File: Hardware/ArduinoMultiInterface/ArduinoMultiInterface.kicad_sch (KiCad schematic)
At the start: 27 parts, among them J1 PORT1, J2 I2C, J3 SPI, J4 SER, SW1 SW_RESET, U1 ATmega328-P, U2 74HC165, U3 74HC595, U4 74HC574, U5 74HC574, U6 74HC574, U7 74HC04, U9 74LS20, Y1 20MHz

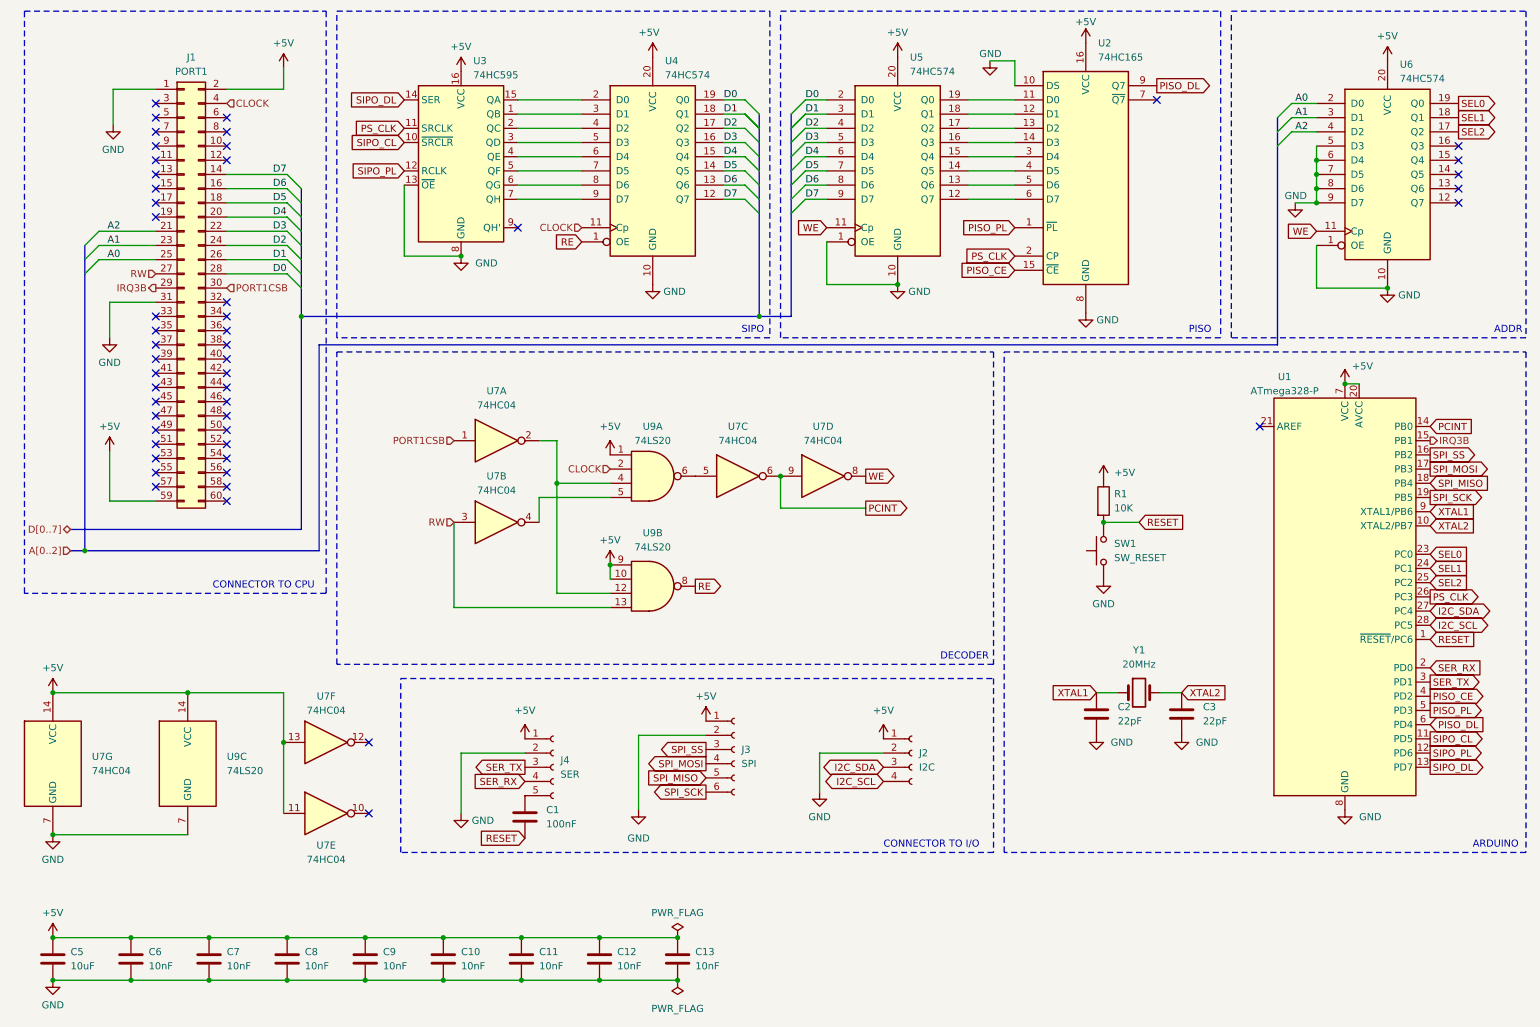
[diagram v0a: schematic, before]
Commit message: Add nfr24l01 protocol
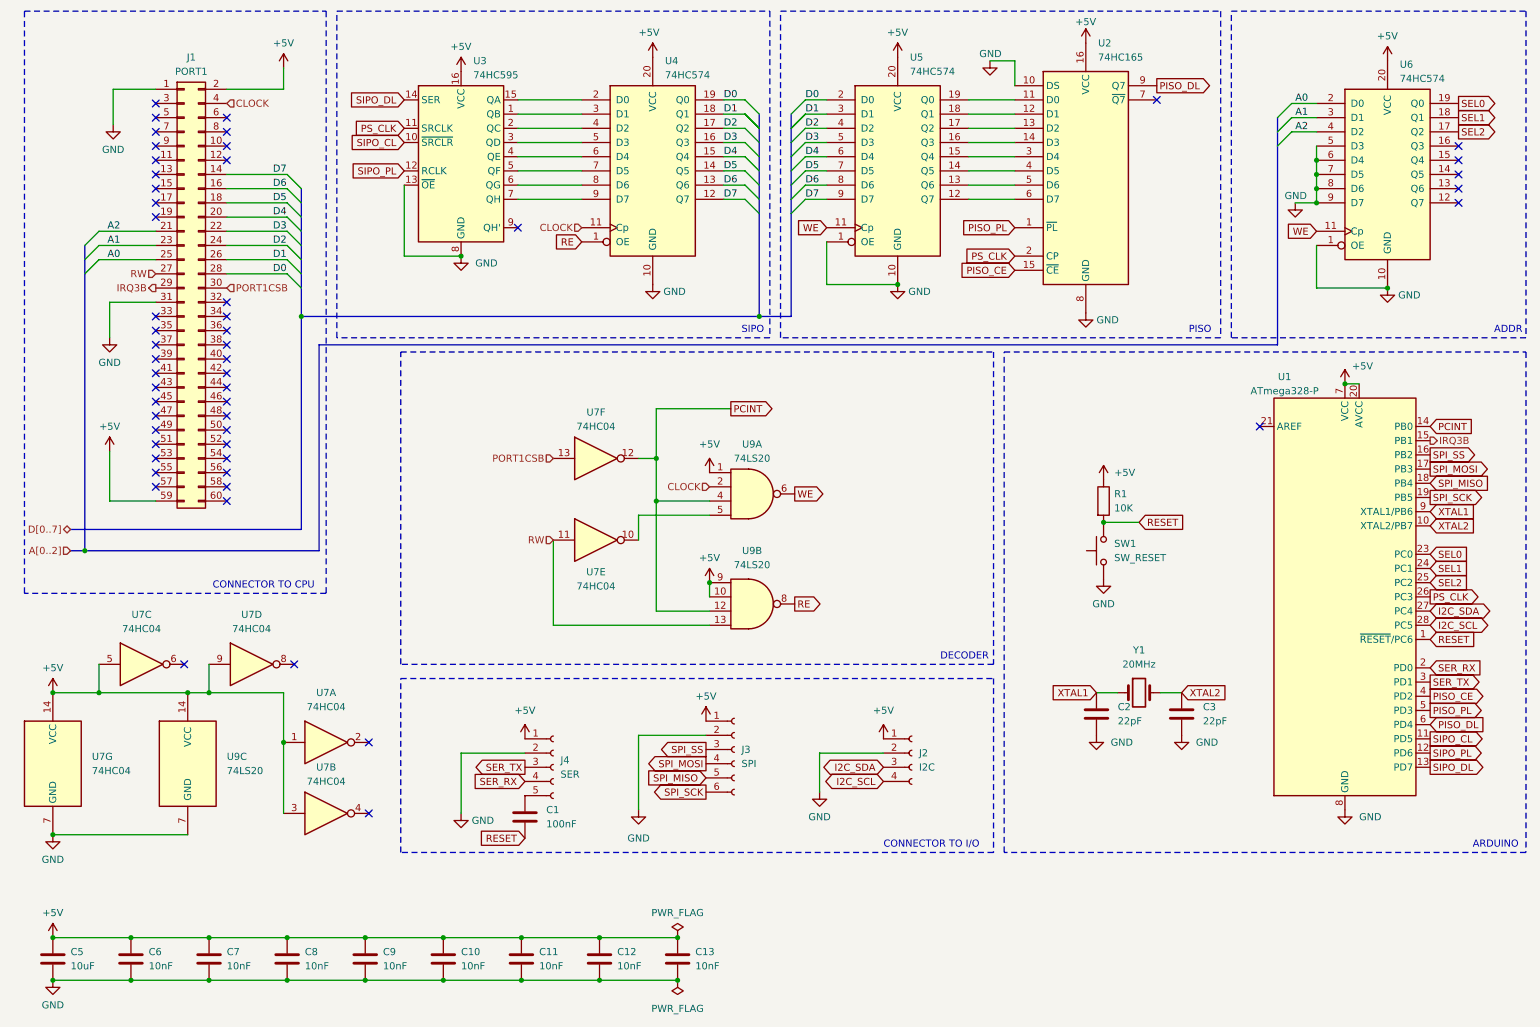
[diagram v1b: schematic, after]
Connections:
- net +5V: now also U7.1, U7.3, U7.5, U7.9; no longer U7.11, U7.13
- net PCINT: now also U7.12, U9.12, U9.4; no longer U7.6, U7.9
- net PORT1CSB: now also U7.13; no longer U7.1
- net RW: now also U7.11; no longer U7.3
- net WE: now also U9.6; no longer U7.8
- net at U9.5: now also U7.10; no longer U7.4
- now unconnected: U7.2
- no-connect marks 51 -> 53
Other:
- moved on the sheet: U7A, U7B, U7C, U7D, U7E, U7F, U9A, U9B

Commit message: Add ArduinoMultiInterface
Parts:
- Y1: footprint Crystal:Crystal_HC18-U_Vertical -> Crystal:Crystal_HC49-4H_Vertical
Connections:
- net +5V: no longer U7.1, U7.3, U7.5, U7.9
- net PCINT: now also U7.8; no longer U7.12, U9.12, U9.4
- net WE: now also U7.1
- net at U7.6: now also U7.9
- net at U7.2: now also U7.3
- net at U7.4: now also U7.5
- new net: U7.12, U9.12, U9.4
- no-connect marks 53 -> 49
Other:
- moved on the sheet: C1, C10, C11, C12, C13, C5, C6, C7, C8, C9, J3, J4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
